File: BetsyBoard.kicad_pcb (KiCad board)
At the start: 4 copper layers, 20.3 x 43.2 mm, 58 parts, among them CON1 SDMMC_Card, P1 USB_OTG, P2 Analog, P3 Digital, P4 JLINK-SWD, P5 VIN, P6 CORTEX-JTAG, P7 RTC, P8 BATT, P9 VDD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

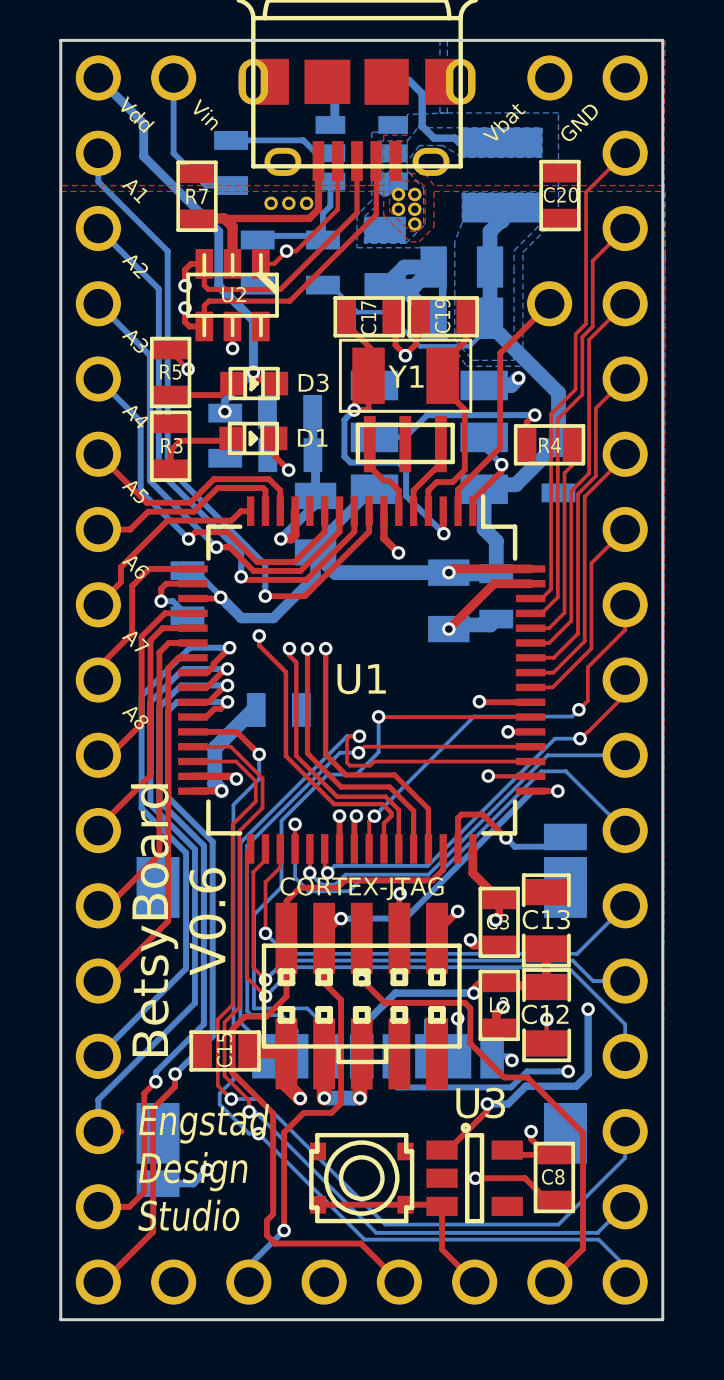
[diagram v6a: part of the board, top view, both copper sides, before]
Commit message: Adding more pin numbers on silkscreen.
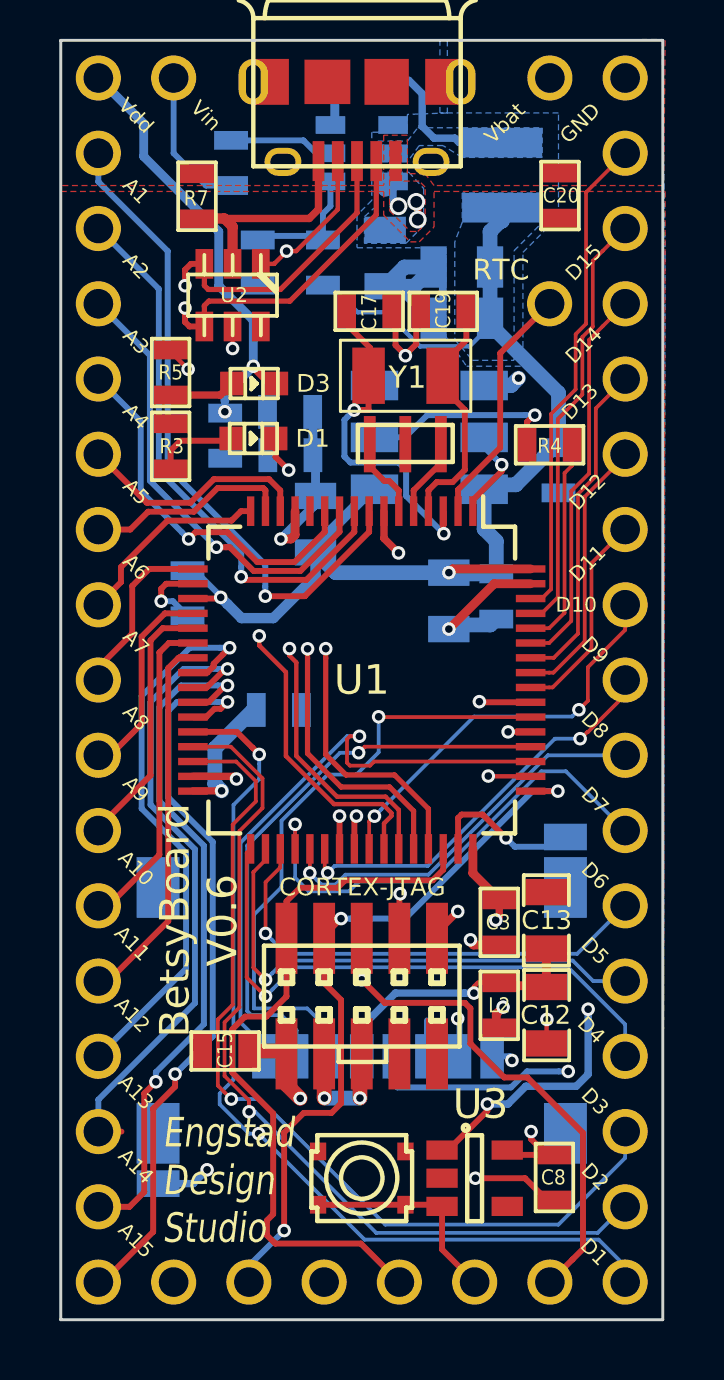
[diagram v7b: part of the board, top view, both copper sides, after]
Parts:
- removed REF** (x8): via, engstad:via-18-10
- R7: footprint SM0603 -> smd:SM0603
- moved C17 0.19 mm to (116.3, 67.6)
- moved C19 0.19 mm to (118.8, 67.6)
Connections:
- P6 pad 7: (no net) -> Net-(P6-Pad7)
- U2 pad 6: (no net) -> Net-(U2-Pad6)
- U3 pad 4: (no net) -> Net-(U3-Pad4)
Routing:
- net VDD: track 103.4 -> 104.8 mm
- net /OTG_5V: track 37.7 -> 38.9 mm, vias 2 -> 5
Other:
- board text added: "A10"
- board text added: "A11"
- board text added: "A12"
- board text added: "A13"
- board text added: "A14"
- board text added: "A15"
- board text added: "D11"
- board text added: "D12"
- board text added: "D13"
- board text added: "D14"
- board text added: "D15"
- board text added: "D3"
- board text added: "D6"
- board text added: "RTC"

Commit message: v0.7
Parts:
- removed C13: 22uF, smd:SM0805
- removed CON1: SDMMC_Card, engstad:SCHD3A0100
- removed L2: 0.47uH, smd:SM0603
- removed P4: JLINK-SWD, engstad:pin-strip-6
- added U5: N25Q00AA, SMD_Packages:SO-16-W, B.Cu at (116.0, 90.7)
- C12: value 22uF -> 0.1uF; footprint smd:SM0805 -> smd:SM0603; moved to B.Cu
- moved D1 28.4 mm to (117.5, 99.9)
- moved R3 28.2 mm to (114.6, 99.9), turned to 180 degrees
- moved C12 4.68 mm to (123.1, 86.8), turned to 90 degrees
- moved C3 0.60 mm to (121.3, 88.3)
- moved C15 0.21 mm to (111.2, 92.6)
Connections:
- C12 pad 1: /VDDSD -> VDD
- U1 pad 53: /SDMMC_CK -> /SDMMC_CLK
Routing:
- net /SDMMC_CK: track 20.1 -> 0.00 mm, vias 2 -> 0
- net VDD: track 104.8 -> 87.5 mm, vias 9 -> 8
- net /JTMS/SWDIO: track 24.6 -> 7.44 mm
- net Earth: track 0.00 -> 15.7 mm
- net /JTDO/SWO: track 30.0 -> 14.9 mm
- net /SDMMC_CLK: track 0.00 -> 14.4 mm, vias 0 -> 1
- net /JTCK/SWCLK: track 24.6 -> 11.6 mm, vias 3 -> 2
- net /SDMMC_D3: track 19.3 -> 6.95 mm
- net /D1: track 44.8 -> 34.6 mm, vias 3 -> 2
- net /VDDSD: track 9.60 -> 0.00 mm, vias 1 -> 0
- net /~MR: track 22.3 -> 14.8 mm, vias 1 -> 0
- net /SDMMC_CMD: track 21.0 -> 16.2 mm, vias 1 -> 2
- net /SDMMC_D0: track 11.1 -> 7.66 mm, vias 2 -> 1
- net GND: track 51.8 -> 48.4 mm, vias 12 -> 11
- net /OTG_FS_ID: track 32.2 -> 28.8 mm
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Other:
- board text added: "BetsyBoard V0.7"
- board text removed: "BetsyBoard V0.6"
- board text removed: "No warranty! Use or reproduce at your own risk!"
- board text removed: "SWO ~RST~ SWD GND CLK VDD"
